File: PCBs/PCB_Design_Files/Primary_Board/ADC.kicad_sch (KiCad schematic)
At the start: 74 parts, among them U11 TMUX1104DGSR, U12 TMUX1133PWR, U13 TMUX1133PWR, U14 TMUX1133PWR, U15 TMUX1133PWR, U7 REF3333AIDBZR, U8 TMUX1133PWR, U9 MCP6561T-E/OT

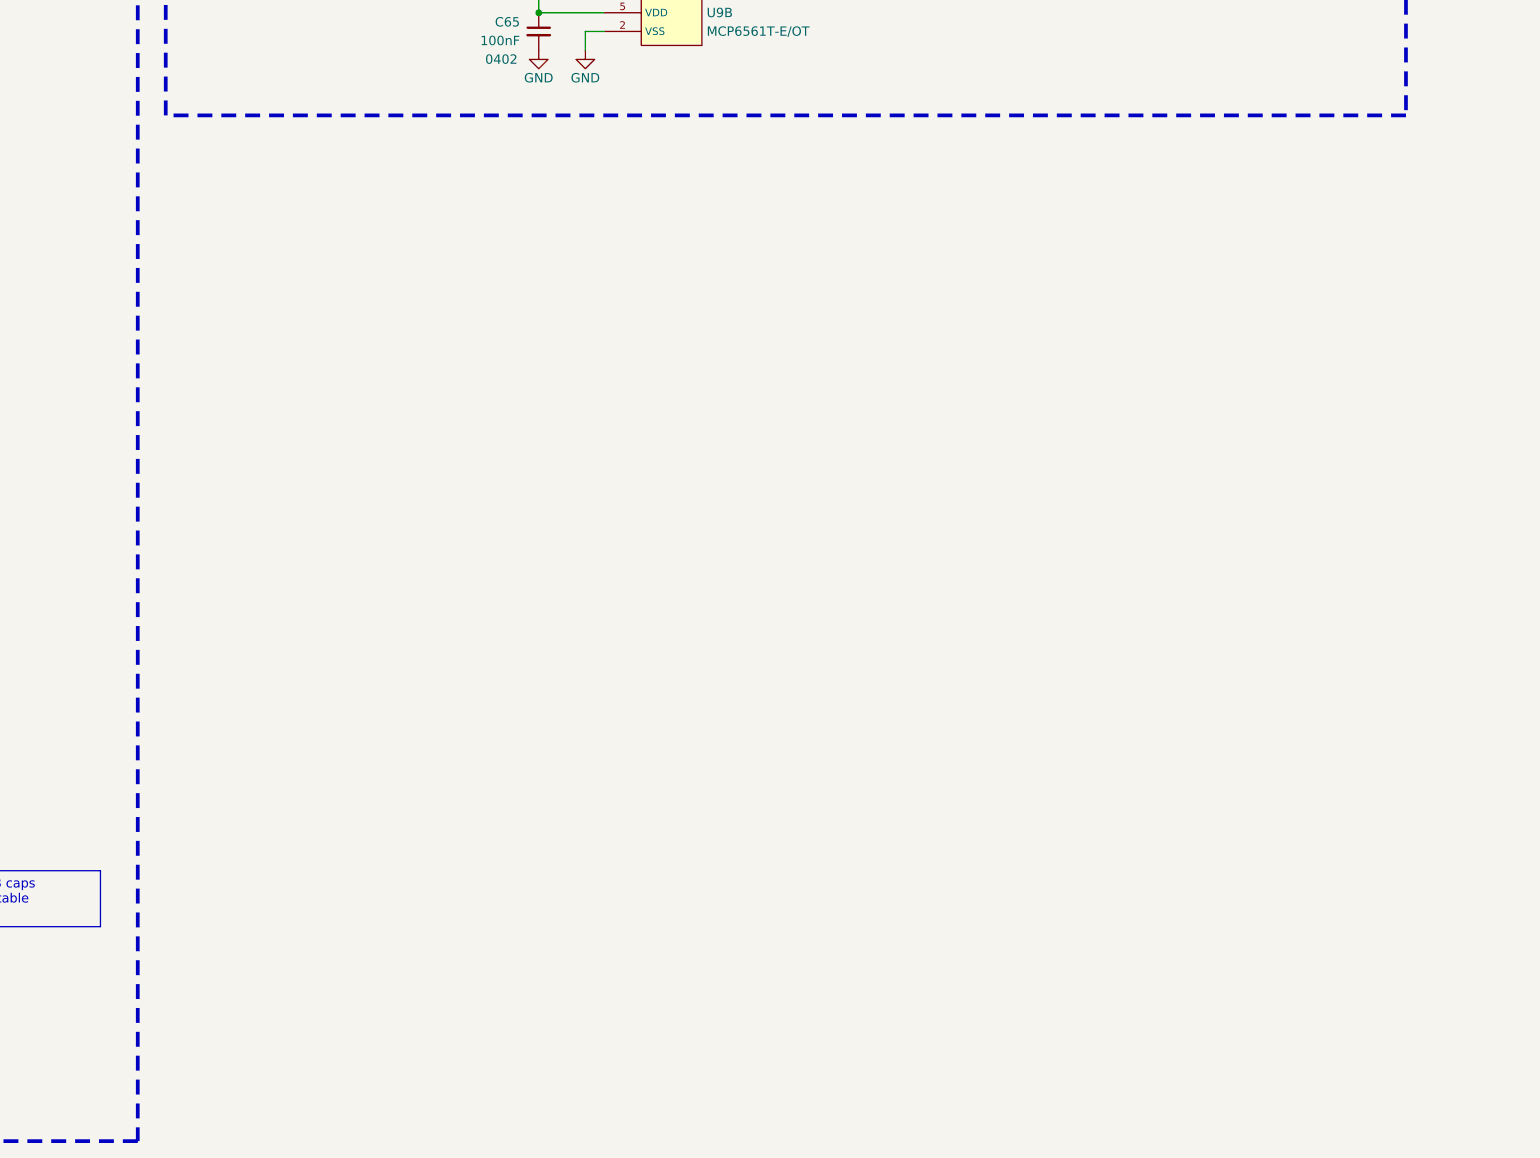
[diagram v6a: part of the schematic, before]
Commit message: Added symbols for Voltage Search DAC
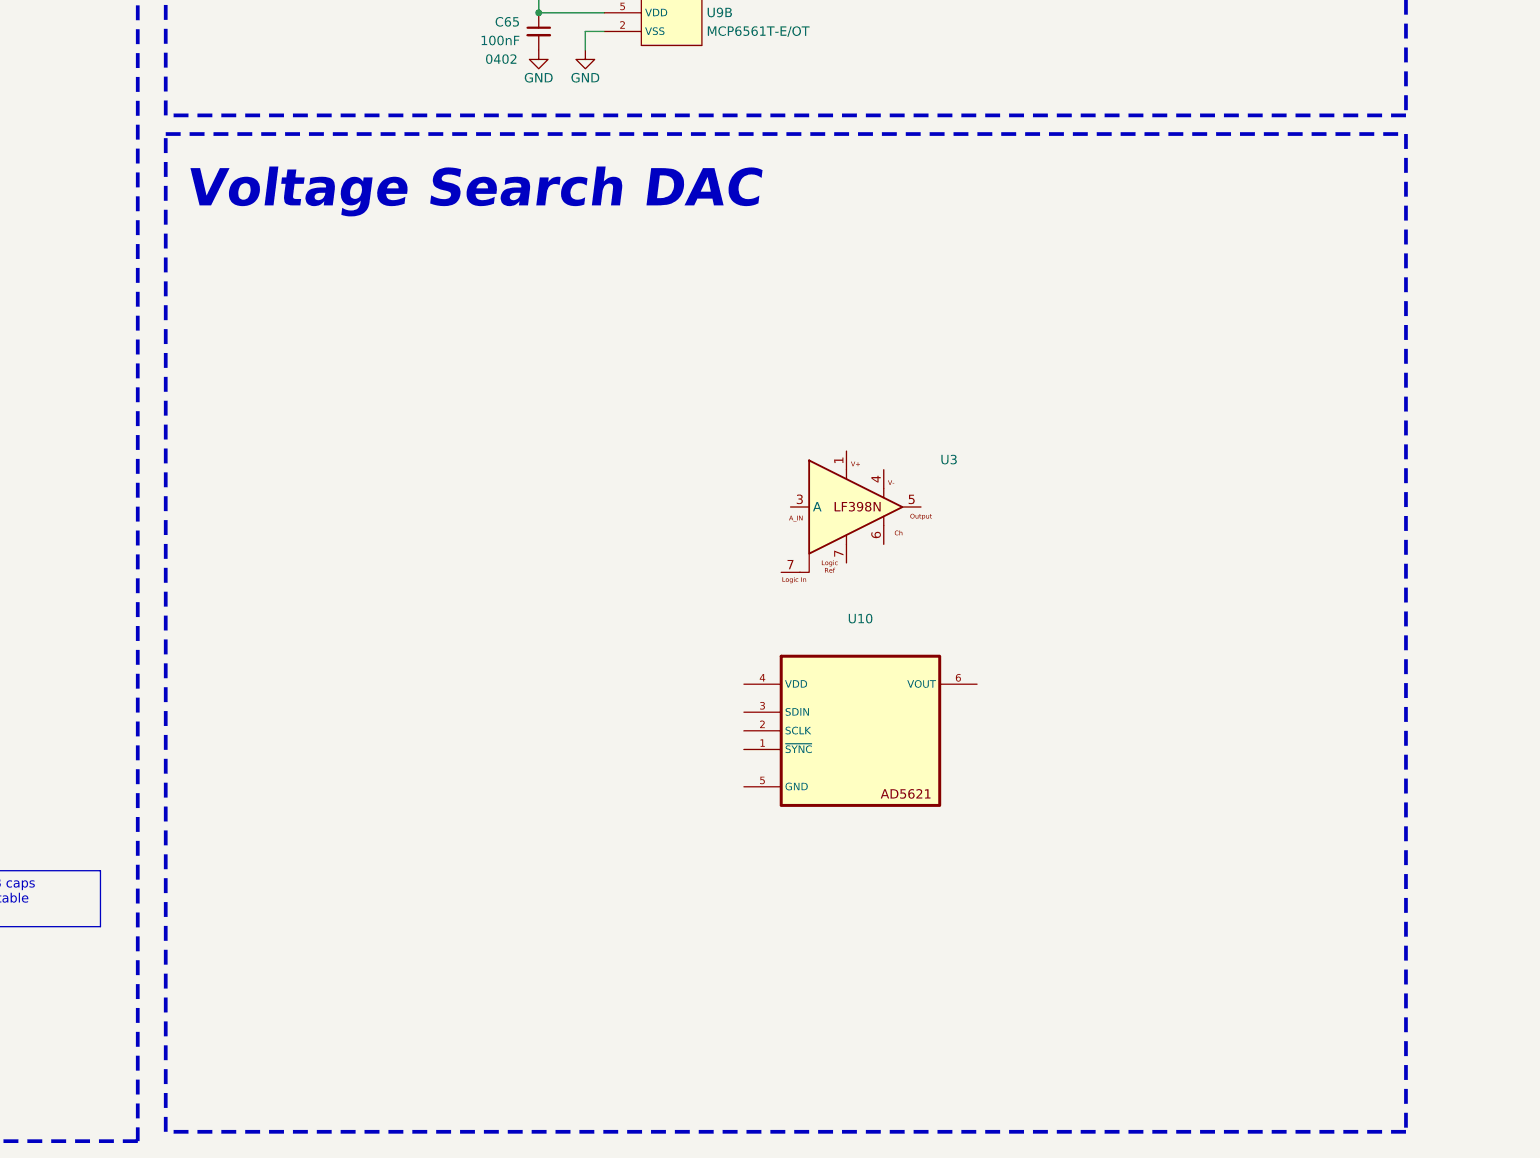
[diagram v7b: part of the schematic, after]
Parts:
- added U10: ~, symbol project_symbols:AD5621AKSZ-REEL7
- added U3: ~, symbol project_symbols:LF398N/NOPB
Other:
- note added: "Voltage Search DAC"
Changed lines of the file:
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@@
 	)
 	(rectangle
+		(start 270.51 254)
+		(end 439.42 389.89)
+		(stroke
+			(width 0.508)
+			(type dash)
+			(color 72 0 0 1)
+		)
+		(fill
+			(type none)
+		)
+	)
+	(rectangle
 		(start 17.78 90.17)
 		(end 266.7 391.16)
@@
 		)
 	)
+	(text "Voltage Search DAC"
+		(exclude_from_sim no)
+		(at 312.42 261.62 0)
+		(effects
+			(font
+				(face "Menlo")
+				(size 5.08 5.08)
+				(bold yes)
+				(italic yes)
+			)
+		)
+	)
 	(text "Bit 0"
 		(exclude_from_sim no)
@@
 	)
 	(symbol
+		(lib_id "project_symbols:LF398N/NOPB")
+		(at 359.41 294.64 0)
+		(unit 1)
+		(exclude_from_sim no)
+		(in_bom yes)
+		(on_board yes)
+		(dnp no)
+		(property "Reference" "U3"
+			(at 377.19 298.3798 0)
+			(effects
+				(font
+					(size 1.27 1.27)
+				)
+			)
+		)
+		(property "Value" "~"
+			(at 377.19 300.9198 0)
+			(effects
+				(font
+					(size 1.27 1.27)
+				)
+			)
+		)
+		(property "Footprint" ""
+			(at 359.41 294.64 0)
+			(effects
+				(font
+					(size 1.27 1.27)
+				)
+				(hide yes)
+			)
+		)
+		(property "Datasheet" ""
+			(at 359.41 294.64 0)
+			(effects
+				(font
+					(size 1.27 1.27)
+				)
+				(hide yes)
+			)
+		)
+		(property "Description" ""
+			(at 359.41 294.64 0)
+			(effects
+				(font
+					(size 1.27 1.27)
+				)
+				(hide yes)
+			)
+		)
+		(pin "5"
+		)
+		(pin "6"
+		)
+		(pin "7"
+		)
+		(pin "7"
+		)
+		(pin "1"
+		)
+		(pin "3"
+		)
+		(pin "4"
+		)
+		(instances
+			(project ""
+				(path "/8c3d01e8-a984-4e4e-9220-7d351336a99b/bd61ebda-1522-4e1f-a5c5-93272ab69f44"
+					(reference "U3")
+					(unit 1)
+				)
+			)
+		)
+	)
+	(symbol
 		(lib_id "Device:C_Small")
 		(at 342.9 45.72 0)
@@
 					(unit 1)
 				)
+			)
+		)
+	)
+	(symbol
+		(lib_id "project_symbols:AD5621AKSZ-REEL7")
+		(at 364.49 323.85 0)
+		(unit 1)
+		(exclude_from_sim no)
+		(in_bom yes)
+		(on_board yes)
+		(dnp no)
+		(fields_autoplaced yes)
+		(property "Reference" "U10"
+			(at 365.125 320.04 0)
+			(effects
+				(font
+					(size 1.27 1.27)
+				)
+			)
+		)
+		(property "Value" "~"
+			(at 365.125 322.58 0)
+			(effects
+				(font
+					(size 1.27 1.27)
+				)
+			)
+		)
+		(property "Footprint" ""
+			(at 364.49 323.85 0)
+			(effects
+				(font
+					(size 1.27 1.27)
+				)
+				(hide yes)
+			)
+		)
+		(property "Datasheet" ""
+			(at 364.49 323.85 0)
+			(effects
+				(font
+					(size 1.27 1.27)
+				)
+				(hide yes)
+			)
+		)
+		(property "Description" ""
+			(at 364.49 323.85 0)
+			(effects
+				(font
+					(size 1.27 1.27)
+				)
+				(hide yes)
+			)
+		)
+		(pin "4"
+		)
+		(pin "6"
+		)
+		(pin "5"
+		)
+		(pin "1"
+		)
+		(pin "2"
+		)
+		(pin "3"
+		)
+		(instances
+			(project ""
+				(path "/8c3d01e8-a984-4e4e-9220-7d351336a99b/bd61ebda-1522-4e1f-a5c5-93272ab69f44"
+					(reference "U10")
+					(unit 1)
+				)

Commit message: Added Voltage Search DAC
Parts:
- removed U10: ~, symbol project_symbols:AD5621AKSZ-REEL7
- removed U3: ~, symbol project_symbols:LF398N/NOPB
- added C64: 100nF, Capacitor_SMD:C_0402_1005Metric, symbol Device:C_Small
- added C65: 1nF, Capacitor_SMD:C_0402_1005Metric, symbol Device:C_Small
- added CAP1, CAP2: CAP, Jumper:SolderJumper-2_P1.3mm_Open_Pad1.0x1.5mm, symbol Jumper:SolderJumper_2_Open
- added R18, R19: 1k, Resistor_SMD:R_0402_1005Metric, symbol Device:R_Small_US
- added R20, R21: 10k, Resistor_SMD:R_0402_1005Metric, symbol Device:R_Small_US
- added S/H1, S/H_EN1, VG1, VG2: TVG, Jumper:SolderJumper-2_P1.3mm_Open_Pad1.0x1.5mm, symbol Jumper:SolderJumper_2_Open
- added U13: LF398N/NOPB, Package_DIP:DIP-8_W7.62mm, symbol project_symbols:LF398N/NOPB
- added U14: AD5621AKSZ, Package_TO_SOT_SMD:SOT-363_SC-70-6, symbol project_symbols:AD5621AKSZ-REEL7
- renumbered JP1 to ADC_BY1, C66 to C10, C67 to C11, C14 to C12, C15 to C13, C16 to C14, C17 to C15, C18 to C16, C19 to C17, C20 to C18, C21 to C19, C22 to C20, C33 to C21, C34 to C22, C35 to C23, C36 to C24, C37 to C25, C38 to C26, C39 to C27, C40 to C28, C12 to C29, C11 to C30, C10 to C31, C13 to C32, C23 to C33, C24 to C34, C25 to C35, C26 to C36, C41 to C37, C42 to C38, C43 to C39, C51 to C4, C44 to C40, C27 to C41, C28 to C42, C45 to C43, C46 to C44, C60 to C45, C29 to C46, C53 to C48, C30 to C49, C48 to C50, C55 to C51, C31 to C52, C49 to C53, C61 to C55, C32 to C56, C50 to C57, C52 to C58, C56 to C59, C62 to C60, C65 to C61, C57 to C62, C58 to C66, C64 to C67, C59 to C69, R16 to R12, R12 to R13, R13 to R14, R14 to R15, R15 to R16, U13 to U10, U9 to U11, U14 to U12, U7 to U3, U11 to U7, U12 to U9
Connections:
- net +3V3A: now also C64.1, U14.4 (VDD)
- net +5V: now also U13.1
- net GND: now also C64.2, C65.2, R19.1, R21.1, U13.4, U13.7, U14.5 (GND)
- net LATCH: now also S/H_EN1.1 (A)
- net MOSI: now also U14.3 (SDIN)
- net MSB_TOP: now also CAP1.1 (A); no longer U11.3 (+)
- net VSMP: now also S/H1.1 (A)
- net V_CM: now also CAP2.1 (A); no longer U11.4 (-)
- net sCLK: now also U14.2 (SCLK)
- net V_COMP: no longer names the net of ADC_BY1.2 (B)
- net V_COMP: now also R20.2; no longer U11.1
- new net: C65.1, U13.6
- new net: R18.2, S/H1.2 (B)
- new net: CAP1.2 (B), U11.3 (+), VG1.2 (B)
- new net: CAP2.2 (B), U11.4 (-), VG2.2 (B)
- new net: S/H_EN1.2 (B), U13.8
- new net ADC_OUT: R20.1, R21.2, U11.1
- new net CS: U14.1 (~{SYNC})
- new net DAC_OUT: U14.6 (VOUT), VG2.1 (A)
- new net S/H_IN: R18.1, R19.2, U13.3 (A)
- new net S/H_OUT: U13.5, VG1.1 (A)
- no-connect marks 3 -> 4
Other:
- moved on the sheet: ADC_BY1, C48, U11A
